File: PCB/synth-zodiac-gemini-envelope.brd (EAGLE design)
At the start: 76.1 x 72.4 mm, 28 parts, among them Q1 PNP, U1 TL074A

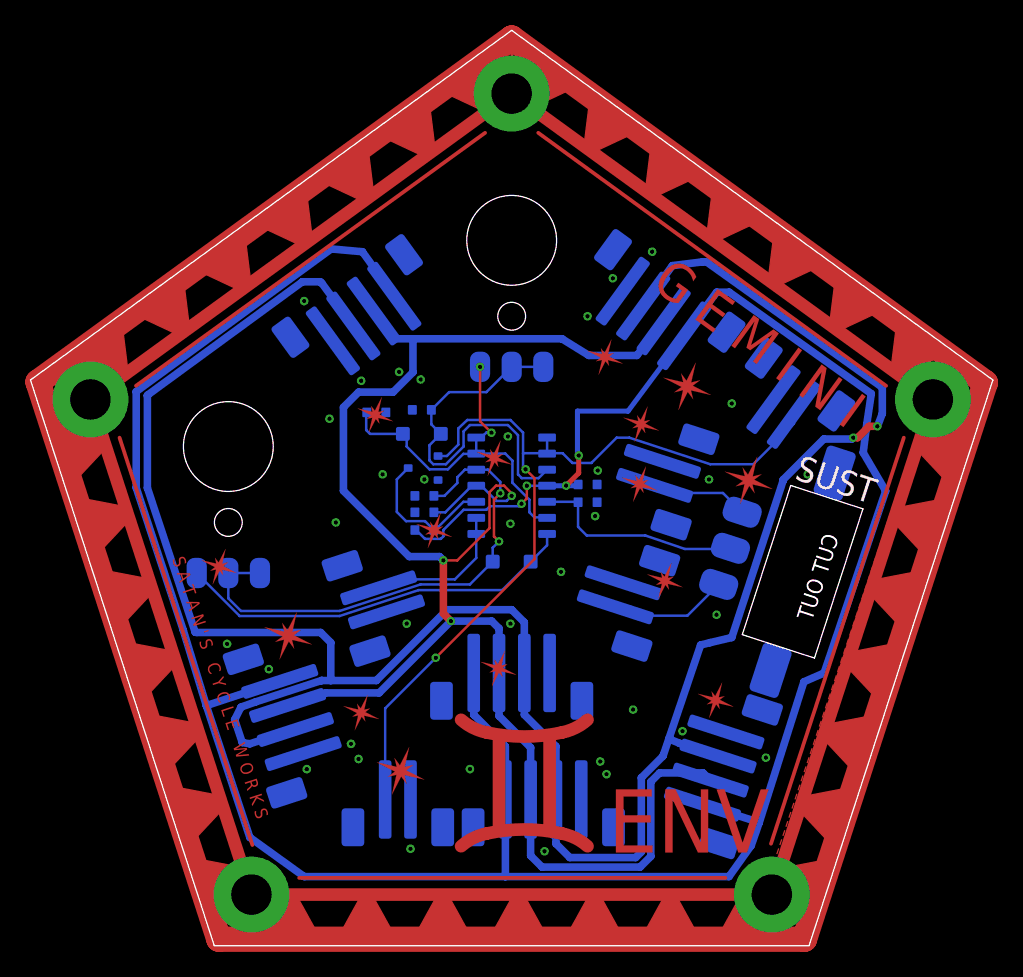
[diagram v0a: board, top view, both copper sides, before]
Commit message: Almost ready for FAB.
Sagittarius was mis-spelled, renamed it.  Taurus is still WIP.
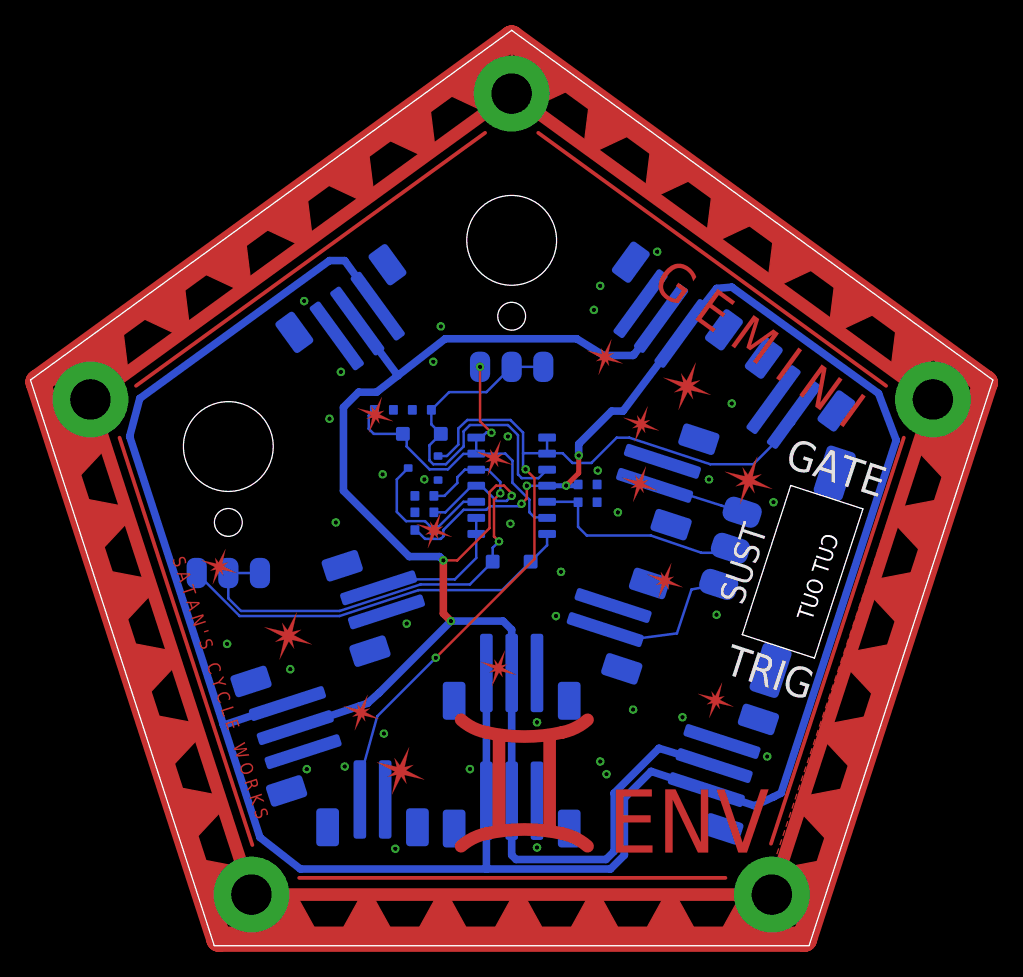
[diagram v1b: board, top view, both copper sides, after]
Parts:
- removed EG_VCF_MOD, TRIG: 2-pin, VT, SMT, con-jst:B2B-PH-SM4
- added EG2VCF_MOD, TRIG_IN: 2-pin, VT, SMT, con-jst:B2B-PH-SM4
- PWR_IN, PWR_LFO, PWR_VCF, PWR_VCF_MOD, PWR_VCO, PWR_VCO_MOD: value (none) -> JST, 3P, VT, SMT; device con-jst:B4B-PH-SM4 -> con-jst:B3B-PH-SM4
- moved PWR_VCF_MOD 2.50 mm to (38.0, 9.90)
- moved PWR_VCF 0.85 mm to (18.8, 17.2)
- moved PWR_VCO_MOD 0.72 mm to (51.1, 52.0)
- moved R2 0.63 mm to (27.9, 43.0)
- moved PWR_VCO 0.54 mm to (24.5, 51.8)
- moved PWR_LFO 0.20 mm to (56.1, 14.2)
- renumbered EG_VCA to EG2VCA, EG_VCO_MOD to EG2VCO_MOD, GATE to GATE_IN
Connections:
- removed net +5V: PWR_IN.3, PWR_LFO.3, PWR_VCF.3, PWR_VCF_MOD.3, PWR_VCO.3, PWR_VCO_MOD.3
- net EG: now also EG2VCF_MOD.1; no longer EG_VCF_MOD.1
- net GND: now also EG2VCF_MOD.2, PWR_IN.3, PWR_LFO.3, PWR_VCF.3, PWR_VCF_MOD.3, PWR_VCO.3, PWR_VCO_MOD.3, TRIG_IN.2; no longer EG_VCF_MOD.2, PWR_IN.4, PWR_LFO.4, PWR_VCF.4, PWR_VCF_MOD.4, PWR_VCO.4, PWR_VCO_MOD.4, TRIG.2
- net TRIG: now also TRIG_IN.1; no longer TRIG.1
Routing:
- net +5V: track 186.6 -> 0.00 mm, vias 2 -> 0
- net +9V: track 223.9 -> 215.2 mm
- net TRIG: track 9.48 -> 11.9 mm
- net GATE: track 7.80 -> 7.27 mm
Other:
- board text added: "ENVELOPE"
- board text added: "GATE"
- board text added: "GEMINI"
- board text added: "Rev. A"
- board text added: "TRIG"

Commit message: Work in progress for rev A,  VCO rev.B
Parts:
- removed EG2VCF_MOD, EG2VCO_MOD: 2-pin, VT, SMT, con-jst:B2B-PH-SM4
- removed PWR_LFO, PWR_VCF, PWR_VCF_MOD, PWR_VCO, PWR_VCO_MOD: JST, 3P, VT, SMT, con-jst:B3B-PH-SM4
- removed SUST: SPDT, switch-thd:SS-12-F45-PNL-SMT
- added EG2VCFMOD, EG2VCOMOD: JST, SH, 2P, con-jst:BM02B-SRSS-TB
- added SRC: (no value), switch-thd:SS-12-F45-PNL-SMT
- EG2VCA, GATE_IN, TRIG_IN: value 2-pin, VT, SMT -> JST, SH, 2P; device con-jst:B2B-PH-SM4 -> con-jst:BM02B-SRSS-TB
- PWR_IN: value JST, 3P, VT, SMT -> JST SM 3P; device con-jst:B3B-PH-SM4 -> con-jst:BM03B-SRSS-TB
- moved GATE_IN 21.0 mm to (55.0, 16.6)
- moved PWR_IN 16.3 mm to (24.0, 11.7)
- moved TRIG_IN 15.3 mm to (53.3, 11.6)
- moved Q1 10.2 mm to (41.2, 38.3)
- moved EG2VCA 9.71 mm to (20.2, 19.3)
- moved R3 6.80 mm to (33.9, 27.3), turned to 180 degrees
- moved C1 5.99 mm to (33.9, 30.9)
- moved C4 5.91 mm to (33.9, 29.7)
- moved U1 5.69 mm to (41.2, 32.3)
- moved C3 5.41 mm to (47.0, 32.6)
- moved R1 5.33 mm to (47.0, 31.3)
- moved D1 5.26 mm to (41.3, 26.9), turned to 180 degrees
- moved R2 4.88 mm to (29.8, 38.5)
- moved C2 4.81 mm to (32.6, 38.5)
- moved D2 4.41 mm to (31.2, 36.7)
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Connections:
- net +9V: no longer PWR_LFO.1, PWR_VCF.1, PWR_VCF_MOD.1, PWR_VCO.1, PWR_VCO_MOD.1
- net -9V: no longer PWR_LFO.2, PWR_VCF.2, PWR_VCF_MOD.2, PWR_VCO.2, PWR_VCO_MOD.2
- net EG: now also EG2VCFMOD.1, EG2VCOMOD.1; no longer EG2VCF_MOD.1, EG2VCO_MOD.1
- net GATE: now also SRC.B; no longer SUST.B
- net GND: now also EG2VCFMOD.2, EG2VCOMOD.2, SRC.MTG1, SRC.MTG2; no longer EG2VCF_MOD.2, EG2VCO_MOD.2, PWR_LFO.3, PWR_VCF.3, PWR_VCF_MOD.3, PWR_VCO.3, PWR_VCO_MOD.3, SUST.MTG1, SUST.MTG2
- net N$134: now also SRC.C; no longer SUST.C
- net TRIG: now also SRC.A; no longer SUST.A
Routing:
- net +9V: track 215.2 -> 38.0 mm, vias 4 -> 3
- net -9V: track 134.7 -> 34.3 mm, vias 3 -> 2
- net EG: track 70.0 -> 37.3 mm, vias 2 -> 0
- net N$136: track 31.8 -> 46.5 mm
- net GATE: track 7.27 -> 21.8 mm
- net EG_VCA: track 11.9 -> 23.7 mm
- net TRIG: track 11.9 -> 20.7 mm
- net N$140: track 11.6 -> 17.7 mm, vias 0 -> 2
- net N$139: track 30.0 -> 34.4 mm, vias 2 -> 0
- net N$137: track 40.5 -> 37.3 mm, vias 2 -> 0
- net N$134: track 17.1 -> 14.1 mm
